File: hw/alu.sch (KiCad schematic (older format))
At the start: 6 parts, among them U701 74HC181, U702 74HC181, U703 74HC182, U704 74HC541, U705 74HC175

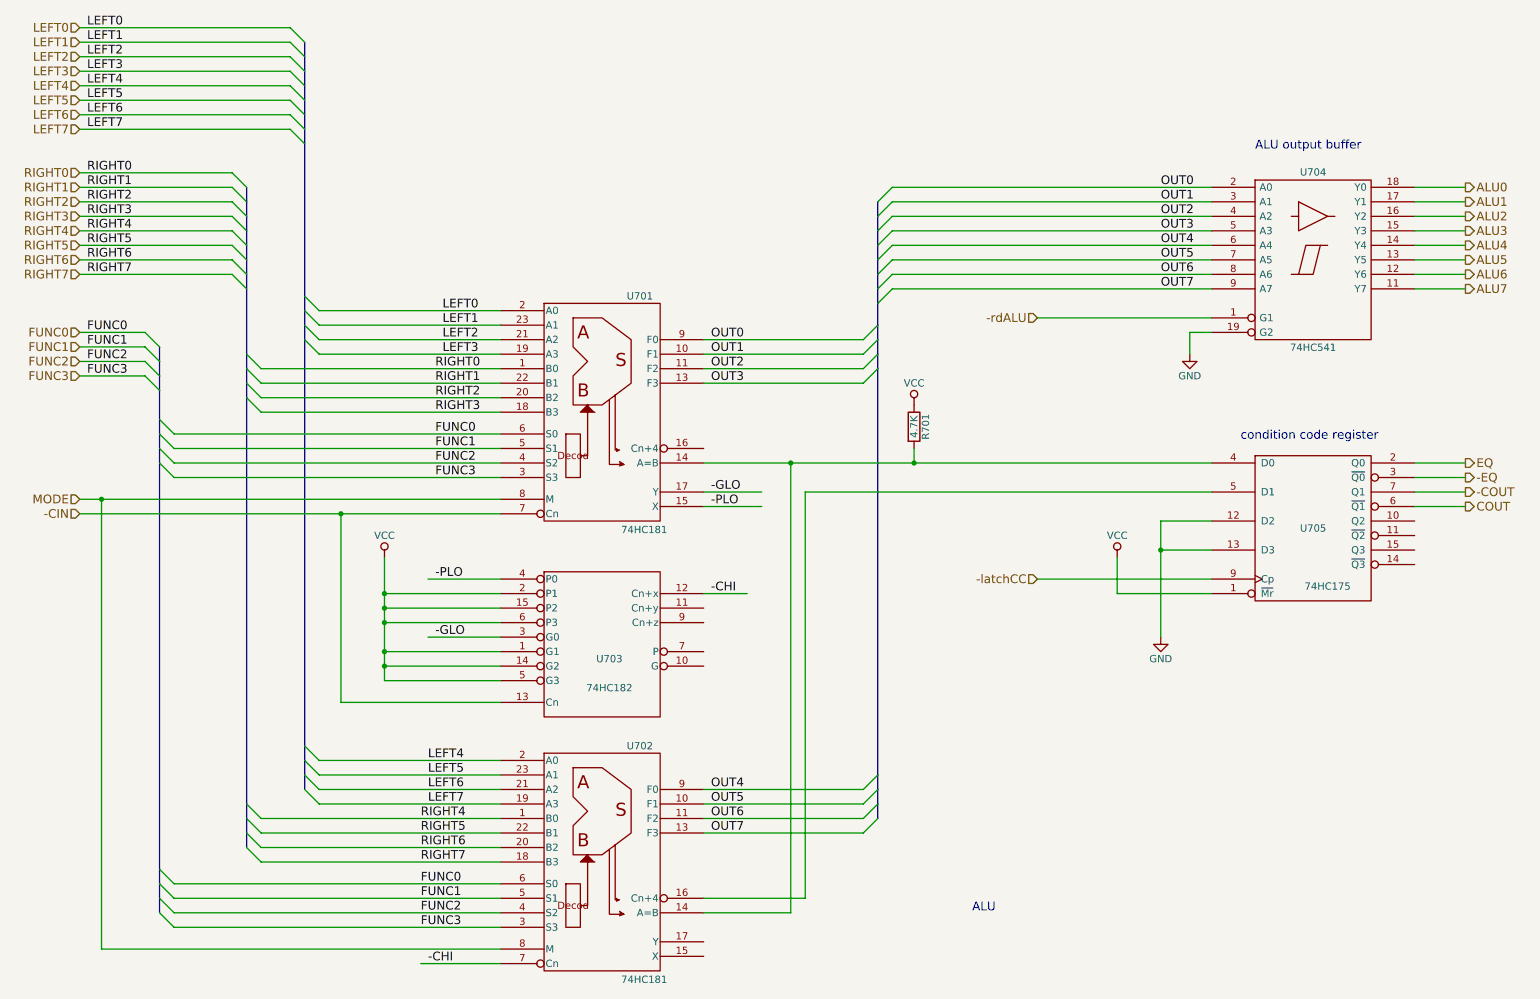
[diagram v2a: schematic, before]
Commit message: allow ALU output to be latched
We can do this with essentially no increase in
complexity, using a '573 latch rather than a '541
buffer for the ALU output.  I'm guessing this
might be useful for some instructions (to hold the
ALU output constant when its inputs might be
changing.)
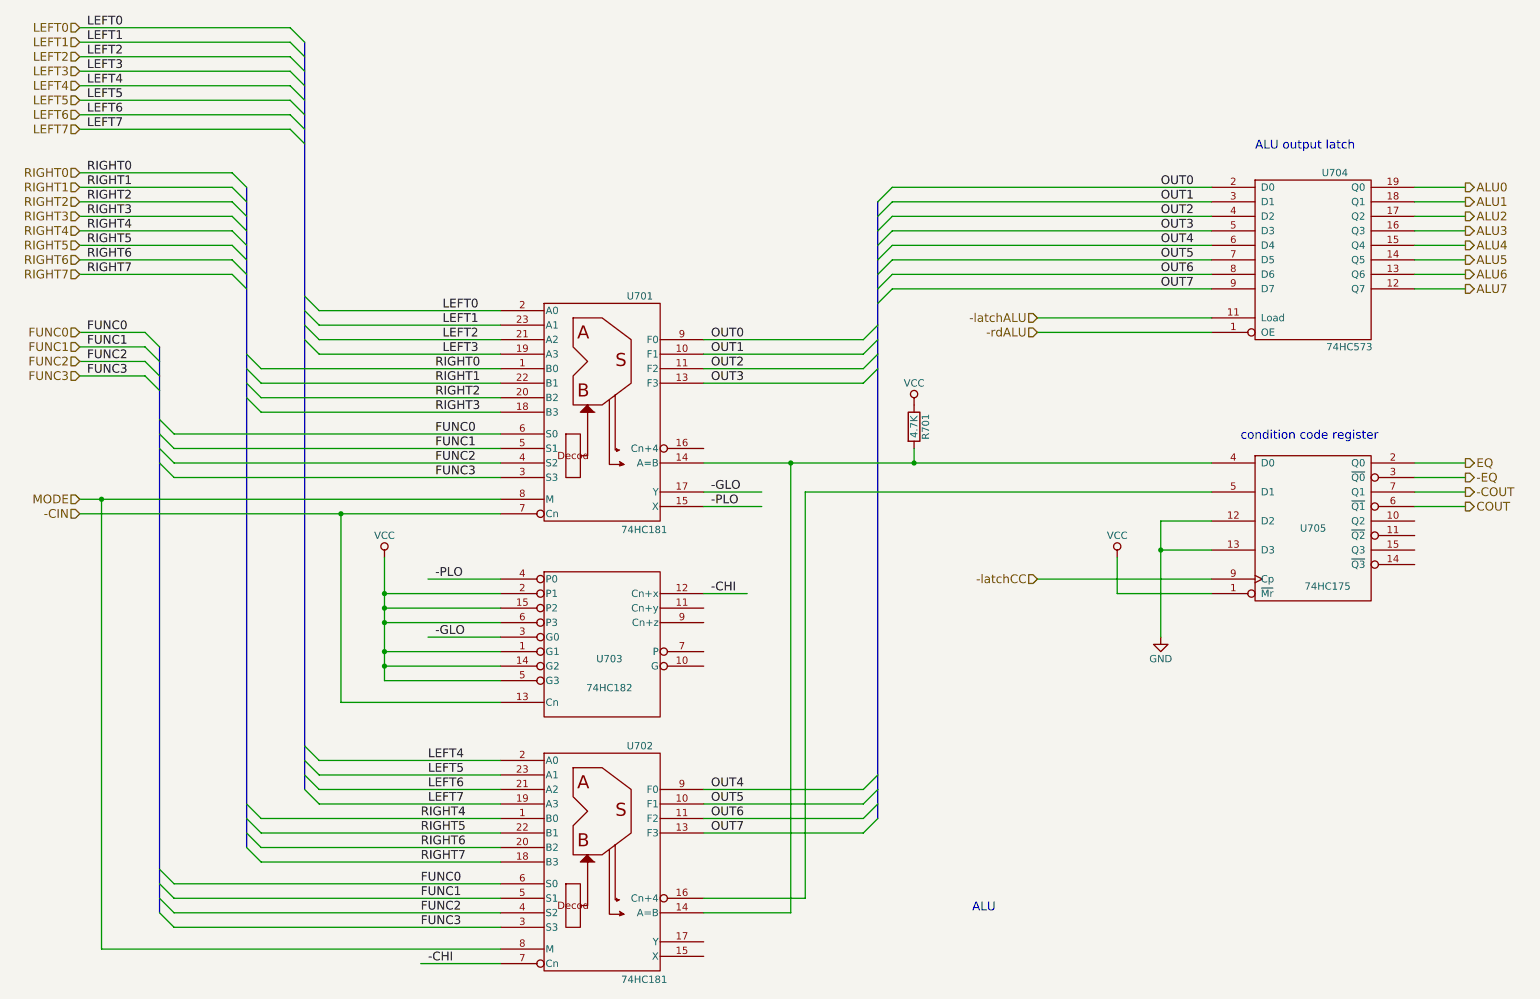
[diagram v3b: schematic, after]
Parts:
- removed U704: 74HC541, symbol 74LS541
- added U704: 74HC573, symbol 74LS573
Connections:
- net labels added: -latchALU
- wire segments 117 -> 106
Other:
- note added: "ALU output latch"
- note removed: "ALU output buffer"
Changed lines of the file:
@@
 Text Label 8450 2450 0    60   ~ 0
 OUT7
-$Comp
-L 74LS541 U704
-U 1 1 5948525C
-P 9500 2250
-F 0 "U704" H 9500 2825 50  0000 C BNN
-F 1 "74HC541" H 9500 1675 50  0000 C TNN
-F 2 "" H 9500 2250 50  0001 C CNN
-F 3 "" H 9500 2250 50  0001 C CNN
-	1    9500 2250
-	1    0    0    -1
-$EndComp
-Text HLabel 7600 2650 0    60   Input ~ 0
+Text HLabel 7600 2750 0    60   Input ~ 0
 -rdALU
-$Comp
-L GND #PWR?
-U 1 1 5948539E
-P 8650 2900
-F 0 "#PWR?" H 8650 2650 50  0001 C CNN
-F 1 "GND" H 8650 2750 50  0000 C CNN
-F 2 "" H 8650 2900 50  0001 C CNN
-F 3 "" H 8650 2900 50  0001 C CNN
-	1    8650 2900
-	1    0    0    -1
-$EndComp
 Text HLabel 10550 1750 2    60   Output ~ 0
 ALU0
@@
 	1000 1350 2450 1350
 Wire Bus Line
-	2550 750  2550 850
-Wire Bus Line
-	2550 850  2550 950
-Wire Bus Line
-	2550 950  2550 1050
-Wire Bus Line
-	2550 1050 2550 1150
-Wire Bus Line
-	2550 1150 2550 1250
-Wire Bus Line
-	2550 1250 2550 1350
-Wire Bus Line
-	2550 1350 2550 1450
-Wire Bus Line
-	2550 1450 2550 2500
-Wire Bus Line
-	2550 2500 2550 2600
-Wire Bus Line
-	2550 2600 2550 2700
-Wire Bus Line
-	2550 2700 2550 2800
-Wire Bus Line
-	2550 2800 2550 5600
-Wire Bus Line
-	2550 5600 2550 5700
-Wire Bus Line
-	2550 5700 2550 5800
-Wire Bus Line
-	2550 5800 2550 5900
+	2550 750  2550 5900
 Wire Wire Line
 	2650 2600 3900 2600
@@
 	1000 2350 2050 2350
 Wire Bus Line
-	2150 1750 2150 1850
-Wire Bus Line
-	2150 1850 2150 1950
-Wire Bus Line
-	2150 1950 2150 2050
-Wire Bus Line
-	2150 2050 2150 2150
-Wire Bus Line
-	2150 2150 2150 2250
-Wire Bus Line
-	2150 2250 2150 2350
-Wire Bus Line
-	2150 2350 2150 2450
-Wire Bus Line
-	2150 2450 2150 2900
-Wire Bus Line
-	2150 2900 2150 3000
-Wire Bus Line
-	2150 3000 2150 3100
-Wire Bus Line
-	2150 3100 2150 3200
-Wire Bus Line
-	2150 3200 2150 6000
-Wire Bus Line
-	2150 6000 2150 6100
-Wire Bus Line
-	2150 6100 2150 6200
-Wire Bus Line
-	2150 6200 2150 6300
+	2150 1750 2150 6300
 Wire Wire Line
 	3900 3000 2250 3000
@@
 	1000 3050 1450 3050
 Wire Bus Line
-	1550 2850 1550 2950
-Wire Bus Line
-	1550 2950 1550 3050
-Wire Bus Line
-	1550 3050 1550 3150
-Wire Bus Line
-	1550 3150 1550 3350
-Wire Bus Line
-	1550 3350 1550 3450
-Wire Bus Line
-	1550 3450 1550 3550
-Wire Bus Line
-	1550 3550 1550 3650
-Wire Bus Line
-	1550 3650 1550 6450
-Wire Bus Line
-	1550 6450 1550 6550
-Wire Bus Line
-	1550 6550 1550 6650
-Wire Bus Line
-	1550 6650 1550 6750
+	1550 2850 1550 6750
 Wire Wire Line
 	3900 3450 1650 3450
@@
 	3900 6850 1650 6850
 Wire Wire Line
-	1000 3900 1150 3900
-Wire Wire Line
-	1150 3900 3900 3900
-Wire Wire Line
-	1000 4000 2800 4000
-Wire Wire Line
-	2800 4000 3900 4000
+	1000 3900 3900 3900
+Wire Wire Line
+	1000 4000 3900 4000
 Wire Wire Line
 	5300 3850 5700 3850
@@
 	5300 6200 6400 6200
 Wire Bus Line
-	6500 1850 6500 1950
-Wire Bus Line
-	6500 1950 6500 2050
-Wire Bus Line
-	6500 2050 6500 2150
-Wire Bus Line
-	6500 2150 6500 2250
-Wire Bus Line
-	6500 2250 6500 2350
-Wire Bus Line
-	6500 2350 6500 2450
-Wire Bus Line
-	6500 2450 6500 2550
-Wire Bus Line
-	6500 2550 6500 2700
-Wire Bus Line
-	6500 2700 6500 2800
-Wire Bus Line
-	6500 2800 6500 2900
-Wire Bus Line
-	6500 2900 6500 3000
-Wire Bus Line
-	6500 3000 6500 5800
-Wire Bus Line
-	6500 5800 6500 5900
-Wire Bus Line
-	6500 5900 6500 6000
-Wire Bus Line
-	6500 6000 6500 6100
+	6500 1850 6500 6100
 Wire Wire Line
 	6600 1750 8800 1750
@@
 	6600 2450 8800 2450
 Wire Wire Line
-	8800 2650 7600 2650
-Wire Wire Line
-	8800 2750 8650 2750
-Wire Wire Line
-	8650 2750 8650 2900
+	8800 2750 7600 2750
 Wire Wire Line
 	10200 1750 10550 1750
@@
 	10200 2450 10550 2450
 Wire Wire Line
-	5300 3650 5900 3650
-Wire Wire Line
-	5900 3650 6750 3650
-Wire Wire Line
-	6750 3650 8800 3650
+	5300 3650 8800 3650
 Wire Wire Line
 	5300 6750 5900 6750
@@
 -COUT
 Wire Wire Line
-	3100 4300 3100 4550
-Wire Wire Line
-	3100 4550 3100 4650
-Wire Wire Line
-	3100 4650 3100 4750
-Wire Wire Line
-	3100 4750 3100 4950
-Wire Wire Line
-	3100 4950 3100 5050
-Wire Wire Line
-	3100 5050 3100 5150
+	3100 4300 3100 5150
 Wire Wire Line
 	2800 5300 2800 4000
@@
 	8800 4050 8450 4050
 Wire Wire Line
-	8450 4050 8450 4250
-Wire Wire Line
-	8450 4250 8450 4850
+	8450 4050 8450 4850
 Wire Wire Line
 	8800 4250 8450 4250
@@
 	7600 4450 8800 4450
 Text Notes 9100 1500 0    60   ~ 0
-ALU output buffer
+ALU output latch
+$Comp
+L 74LS573 U704
+U 1 1 599710FF
+P 9500 2250
+F 0 "U704" H 9650 2850 50  0000 C CNN
+F 1 "74HC573" H 9750 1650 50  0000 C CNN
+F 2 "" H 9500 2250 50  0001 C CNN
+F 3 "" H 9500 2250 50  0001 C CNN
+	1    9500 2250
+	1    0    0    -1
+$EndComp
+Wire Wire Line
+	8800 2650 7600 2650
+Text HLabel 7600 2650 0    60   Input ~ 0
+-latchALU
 $EndSCHEMATC
